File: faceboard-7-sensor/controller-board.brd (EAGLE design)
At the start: 45.7 x 56.8 mm, 11 parts

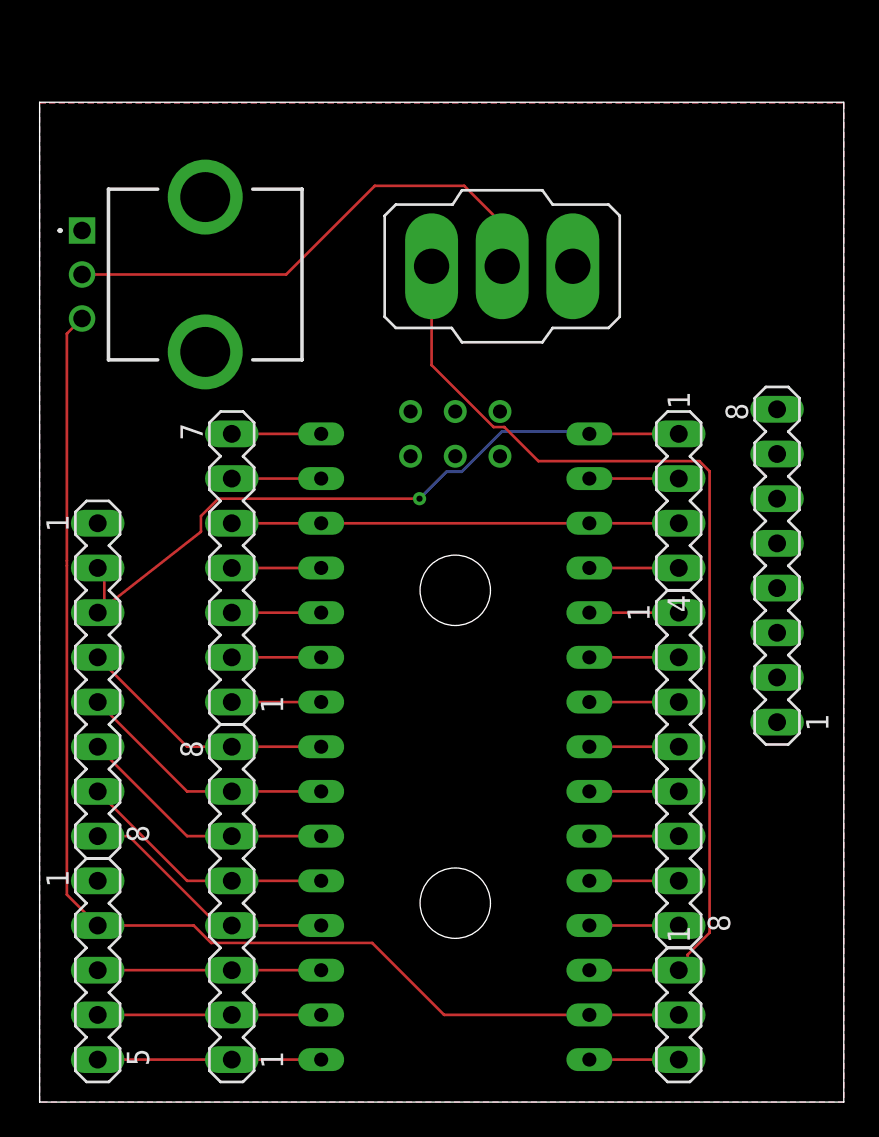
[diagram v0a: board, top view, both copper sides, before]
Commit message: add ffc boards
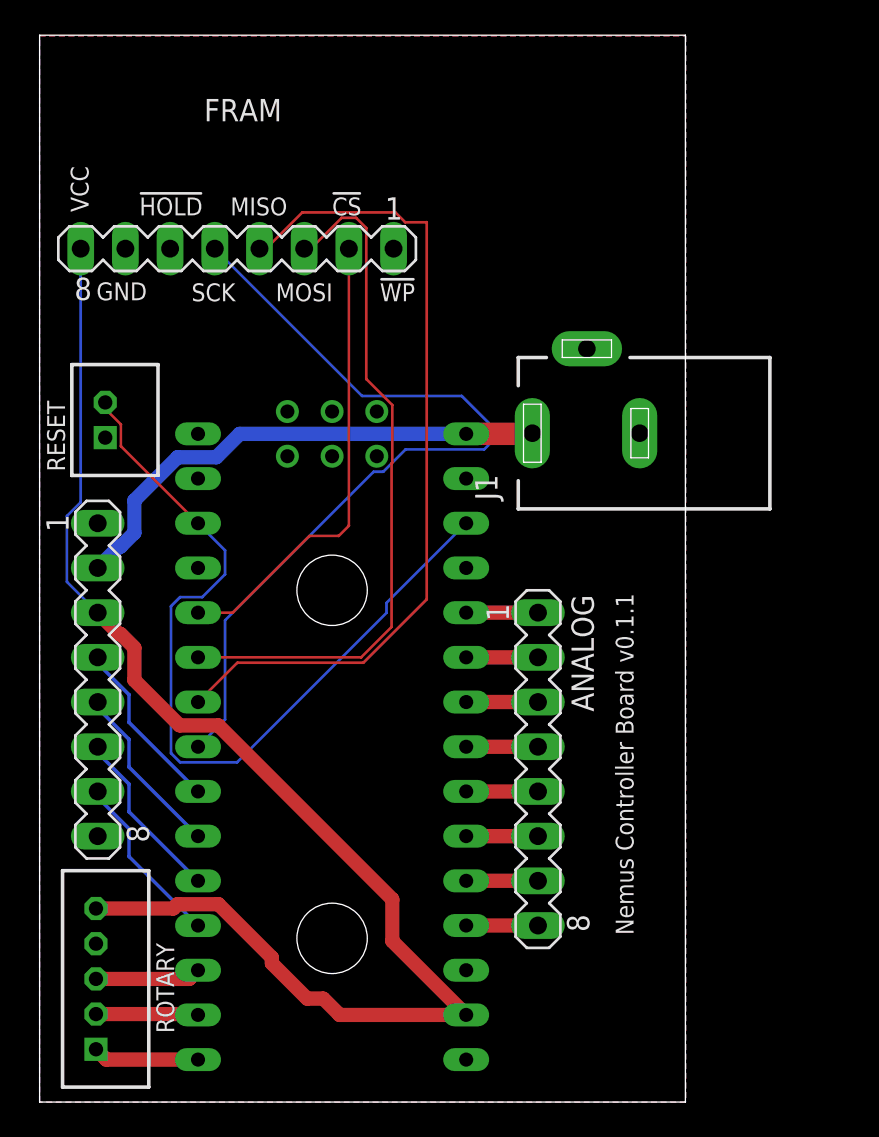
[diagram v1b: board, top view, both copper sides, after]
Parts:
- removed S1: (no value), switch:320-916
- removed SV1: SIGNALS, con-lstb:MA08-1
- removed SV3: ROTARY, con-lstb:MA05-1
- removed SV4: ARDUINO13, con-lstb:MA03-1
- removed SV5: ARDUINOVUSB, con-lstb:MA04-1
- removed SV6: HEADER, con-lstb:MA08-1
- removed SV7: ARDUINO4, con-lstb:MA07-1
- removed SV8: ARDUINO12, con-lstb:MA08-1
- removed VR1: PTV09A-4225F-B203, PTV09A-4225F-B203:PTV09A4225FB203
- added ANALOG: SIGNALS, con-lstb:MA08-1
- added FRAM: FRAM, con-lstb:MA08-1
- added J1: DCJ0202, con-jack:DCJ0202
- added RESET: B2B-PH-K, con-jst-ph:B2B-PH-K
- added ROTARY: B5B-PH-K, con-jst-ph:B5B-PH-K
- moved U$1 7.00 mm to (14.1, 29.1)
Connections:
- removed net 3.3V: SV3.2, SV4.2, U$1.3.3V, VR1.3
- removed net D: SV2.7, SV8.5, U$1.D8
- removed net D2: SV7.3, U$1.D2
- removed net D3: SV7.2, U$1.D3
- removed net INT: SV7.1, U$1.D4
- removed net N$10: S1.2, VR1.2
- removed net RCLK: SV3.5, SV8.1, U$1.D12
- removed net RDATA: SV3.4, SV8.2, U$1.D11
- removed net RSW: SV3.3, SV8.3, U$1.D10
- new net 3V: FRAM.8, ROTARY.5, SV2.3, U$1.3.3V
- new net FRAM_CLK: FRAM.5, U$1.D5
- new net FRAM_CS: FRAM.2, U$1.D2
- new net FRAM_MISO: FRAM.4, U$1.D4
- new net FRAM_MOSI: FRAM.3, U$1.D3
- new net N$3: FRAM.6
- new net N$8: FRAM.1
- new net ROTA: ROTARY.3, U$1.D10
- new net ROTB: ROTARY.2, U$1.D11
- new net ROTC: ROTARY.1, U$1.D12
- net A: now also U$1.D6; no longer SV8.8, U$1.D5
- net A0: now also ANALOG.8; no longer SV1.8
- net A1: now also ANALOG.7; no longer SV1.7
- net A2: now also ANALOG.6; no longer SV1.6
- net A3: now also ANALOG.5; no longer SV1.5
- net A4: now also ANALOG.4; no longer SV1.4
- net A5: now also ANALOG.3; no longer SV1.3
- net A6: now also ANALOG.2; no longer SV1.2
- net A7: now also ANALOG.1; no longer SV1.1
- net AREF: no longer S1.3, SV4.1
- net B: now also U$1.D7; no longer SV8.7, U$1.D6
- net C: now also U$1.D8; no longer SV8.6, U$1.D7
- net D0: no longer SV7.7
- net D1: no longer SV7.6
- net D13: no longer SV4.3
- net GND: now also FRAM.7, J1.2, J1.3, RESET.1, ROTARY.4; no longer SV3.1, SV5.2, SV7.4, VR1.1, VR1.MH1, VR1.MH2
- net LEDDATA: now also SV2.7; no longer SV2.8, SV8.4
- net RST: now also RESET.2; no longer SV5.3, SV7.5
- net VIN: now also J1.1; no longer SV2.3, SV5.1
- net VUSB: no longer SV5.4
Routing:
- net 3V: track 0.00 -> 78.5 mm
- net 3.3V: track 70.7 -> 0.00 mm
- net AREF: track 58.3 -> 0.00 mm
- net FRAM_CLK: track 0.00 -> 48.1 mm
- net FRAM_MISO: track 0.00 -> 47.4 mm
- net FRAM_MOSI: track 0.00 -> 39.5 mm
- net N$10: track 29.3 -> 0.00 mm
- net FRAM_CS: track 0.00 -> 26.4 mm
- net RST: track 25.4 -> 47.7 mm
- net D: track 14.8 -> 0.00 mm
- net RSW: track 12.7 -> 0.00 mm
- net RDATA: track 12.7 -> 0.00 mm
- net RCLK: track 12.7 -> 0.00 mm
- net VIN: track 39.9 -> 28.9 mm, vias 1 -> 0
- net GND: track 10.2 -> 0.00 mm
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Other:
- board size 45.7 x 56.8 mm -> 36.7 x 60.6 mm
- board text added: "!CS"
- board text added: "!HOLD"
- board text added: "!WP"
- board text added: "/Users/admin/Documents/EAGLE/projects/haptic-harpsichord-cad/logo/logobw_small.bmp"
- board text added: "MISO"
- board text added: "MOSI"
- board text added: "Nemus Controller Board v0.1.1"
- board text added: "SCK"
- board text added: "VCC"
- board text removed: "3.3V"
- board text removed: "AREF"
- board text removed: "AREF POT"
- board text removed: "ATTENZIONE"
- board text removed: "D"
- board text removed: "RCLK"
- board text removed: "RDATA"
- board text removed: "RSW"
